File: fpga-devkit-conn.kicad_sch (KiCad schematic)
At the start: 12 parts, among them J13 PinHeader_2x10_P1.27mm_SMD_Sh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, J14 PinHeader_2x10_P1.27mm_SMD_Sh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

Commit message: [#83609] Reannotate board
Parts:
- renumbered J13 to J12, J14 to J13, R232 to R317, R233 to R318, R234 to R319, R235 to R320, R236 to R321, R237 to R322, R238 to R323, R239 to R324, R276 to R325, R277 to R326
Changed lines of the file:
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@@
 		(dnp no)
 		(fields_autoplaced yes)
-		(property "Reference" "J13"
+		(property "Reference" "J12"
 			(at 240.9825 173.99 0)
 			(effects
@@
 			(project "bmc-reference-carrier-board"
 				(path "/5f636c45-3c15-4731-8931-4625e0dab7e4/3ed11a6c-c41e-4496-8ded-d9f7860b25fe"
-					(reference "J13")
+					(reference "J12")
 					(unit 1)
 				)
@@
 		(on_board yes)
 		(dnp yes)
-		(property "Reference" "R232"
+		(property "Reference" "R317"
 			(at 150.368 90.424 0)
 			(effects
@@
 			(project "bmc-reference-carrier-board"
 				(path "/5f636c45-3c15-4731-8931-4625e0dab7e4/3ed11a6c-c41e-4496-8ded-d9f7860b25fe"
-					(reference "R232")
+					(reference "R317")
 					(unit 1)
 				)
@@
 		(on_board yes)
 		(dnp yes)
-		(property "Reference" "R236"
+		(property "Reference" "R321"
 			(at 150.368 105.664 0)
 			(effects
@@
 			(project "bmc-reference-carrier-board"
 				(path "/5f636c45-3c15-4731-8931-4625e0dab7e4/3ed11a6c-c41e-4496-8ded-d9f7860b25fe"
-					(reference "R236")
+					(reference "R321")
 					(unit 1)
 				)
@@
 		(on_board yes)
 		(dnp yes)
-		(property "Reference" "R276"
+		(property "Reference" "R325"
 			(at 165.1 221.615 0)
 			(effects
@@
 			(project "bmc-reference-carrier-board"
 				(path "/5f636c45-3c15-4731-8931-4625e0dab7e4/3ed11a6c-c41e-4496-8ded-d9f7860b25fe"
-					(reference "R276")
+					(reference "R325")
 					(unit 1)
 				)
@@
 		(on_board yes)
 		(dnp no)
-		(property "Reference" "#PWR0301"
+		(property "Reference" "#PWR0373"
 			(at 256.54 207.01 0)
 			(effects
@@
 			(project "bmc-reference-carrier-board"
 				(path "/5f636c45-3c15-4731-8931-4625e0dab7e4/3ed11a6c-c41e-4496-8ded-d9f7860b25fe"
-					(reference "#PWR0301")
+					(reference "#PWR0373")
 					(unit 1)
 				)
@@
 		(on_board yes)
 		(dnp no)
-		(property "Reference" "#PWR0270"
+		(property "Reference" "#PWR0374"
 			(at 259.08 119.38 0)
 			(effects
@@
 			(project "bmc-reference-carrier-board"
 				(path "/5f636c45-3c15-4731-8931-4625e0dab7e4/3ed11a6c-c41e-4496-8ded-d9f7860b25fe"
-					(reference "#PWR0270")
+					(reference "#PWR0374")
 					(unit 1)
 				)
@@
 		(on_board yes)
 		(dnp no)
-		(property "Reference" "#PWR0267"
+		(property "Reference" "#PWR0371"
 			(at 243.84 119.38 0)
 			(effects
@@
 			(project "bmc-reference-carrier-board"
 				(path "/5f636c45-3c15-4731-8931-4625e0dab7e4/3ed11a6c-c41e-4496-8ded-d9f7860b25fe"
-					(reference "#PWR0267")
+					(reference "#PWR0371")
 					(unit 1)
 				)
@@
 		(on_board yes)
 		(dnp yes)
-		(property "Reference" "R239"
+		(property "Reference" "R324"
 			(at 150.368 115.824 0)
 			(effects
@@
 			(project "bmc-reference-carrier-board"
 				(path "/5f636c45-3c15-4731-8931-4625e0dab7e4/3ed11a6c-c41e-4496-8ded-d9f7860b25fe"
-					(reference "R239")
+					(reference "R324")
 					(unit 1)
 				)
@@
 		(on_board yes)
 		(dnp yes)
-		(property "Reference" "R237"
+		(property "Reference" "R322"
 			(at 150.368 108.204 0)
 			(effects
@@
 			(project "bmc-reference-carrier-board"
 				(path "/5f636c45-3c15-4731-8931-4625e0dab7e4/3ed11a6c-c41e-4496-8ded-d9f7860b25fe"
-					(reference "R237")
+					(reference "R322")
 					(unit 1)
 				)
@@
 		(on_board yes)
 		(dnp yes)
-		(property "Reference" "R238"
+		(property "Reference" "R323"
 			(at 150.368 113.284 0)
 			(effects
@@
 			(project "bmc-reference-carrier-board"
 				(path "/5f636c45-3c15-4731-8931-4625e0dab7e4/3ed11a6c-c41e-4496-8ded-d9f7860b25fe"
-					(reference "R238")
+					(reference "R323")
 					(unit 1)
 				)
@@
 		(on_board yes)
 		(dnp yes)
-		(property "Reference" "R235"
+		(property "Reference" "R320"
 			(at 150.368 100.584 0)
 			(effects
@@
 			(project "bmc-reference-carrier-board"
 				(path "/5f636c45-3c15-4731-8931-4625e0dab7e4/3ed11a6c-c41e-4496-8ded-d9f7860b25fe"
-					(reference "R235")
+					(reference "R320")
 					(unit 1)
 				)
@@
 		(on_board yes)
 		(dnp yes)
-		(property "Reference" "R277"
+		(property "Reference" "R326"
 			(at 165.1 224.155 0)
 			(effects
@@
 			(project "bmc-reference-carrier-board"
 				(path "/5f636c45-3c15-4731-8931-4625e0dab7e4/3ed11a6c-c41e-4496-8ded-d9f7860b25fe"
-					(reference "R277")
+					(reference "R326")
 					(unit 1)
 				)
@@
 		(on_board yes)
 		(dnp yes)
-		(property "Reference" "R233"
+		(property "Reference" "R318"
 			(at 150.368 92.964 0)
 			(effects
@@
 			(project "bmc-reference-carrier-board"
 				(path "/5f636c45-3c15-4731-8931-4625e0dab7e4/3ed11a6c-c41e-4496-8ded-d9f7860b25fe"
-					(reference "R233")
+					(reference "R318")
 					(unit 1)
 				)
@@
 		(on_board yes)
 		(dnp yes)
-		(property "Reference" "R234"
+		(property "Reference" "R319"
 			(at 150.368 98.044 0)
 			(effects
@@
 			(project "bmc-reference-carrier-board"
 				(path "/5f636c45-3c15-4731-8931-4625e0dab7e4/3ed11a6c-c41e-4496-8ded-d9f7860b25fe"
-					(reference "R234")
+					(reference "R319")
 					(unit 1)
 				)
@@
 		(dnp no)
 		(fields_autoplaced yes)
-		(property "Reference" "J14"
+		(property "Reference" "J13"
 			(at 242.2525 85.09 0)
 			(effects
@@
 			(project "bmc-reference-carrier-board"
 				(path "/5f636c45-3c15-4731-8931-4625e0dab7e4/3ed11a6c-c41e-4496-8ded-d9f7860b25fe"
-					(reference "J14")
+					(reference "J13")
 					(unit 1)
 				)
@@
 		(on_board yes)
 		(dnp no)
-		(property "Reference" "#PWR0271"
+		(property "Reference" "#PWR0372"
 			(at 243.84 207.01 0)
 			(effects
@@
 			(project "bmc-reference-carrier-board"
 				(path "/5f636c45-3c15-4731-8931-4625e0dab7e4/3ed11a6c-c41e-4496-8ded-d9f7860b25fe"
-					(reference "#PWR0271")
+					(reference "#PWR0372")
 					(unit 1)
 				)

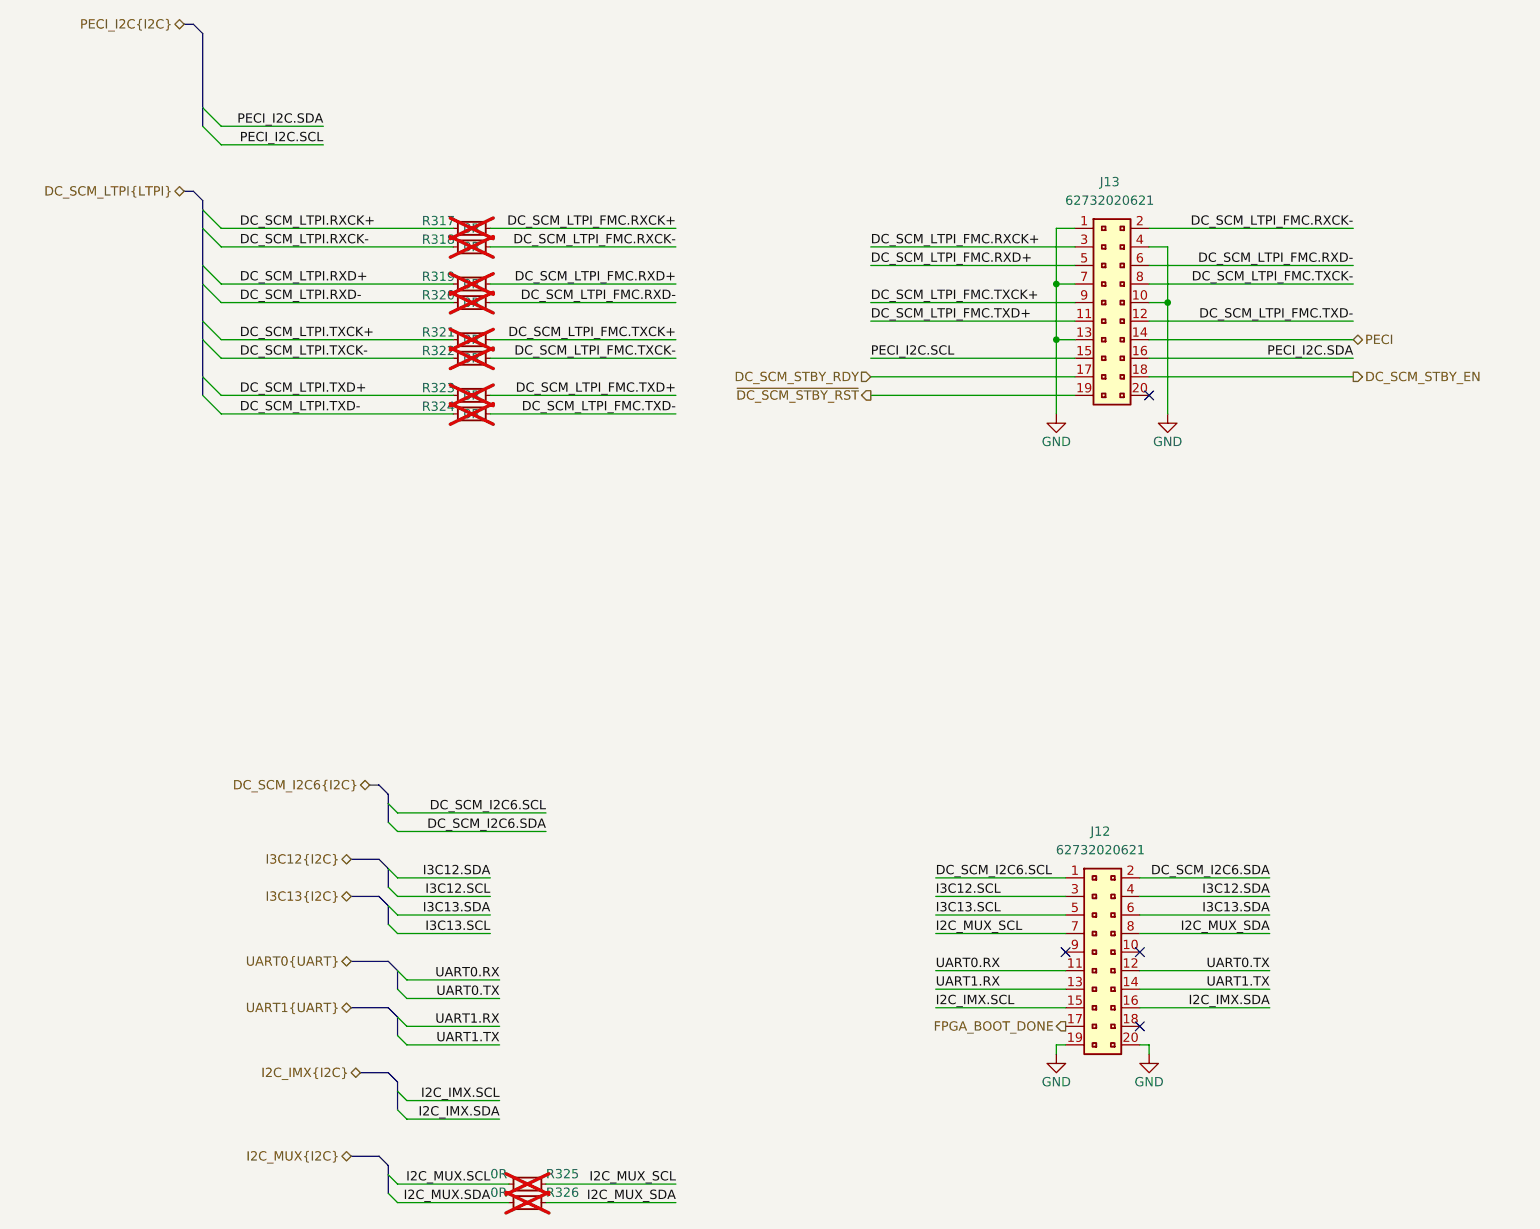
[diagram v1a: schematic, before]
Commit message: [#83736] Update devkit connectors pinout
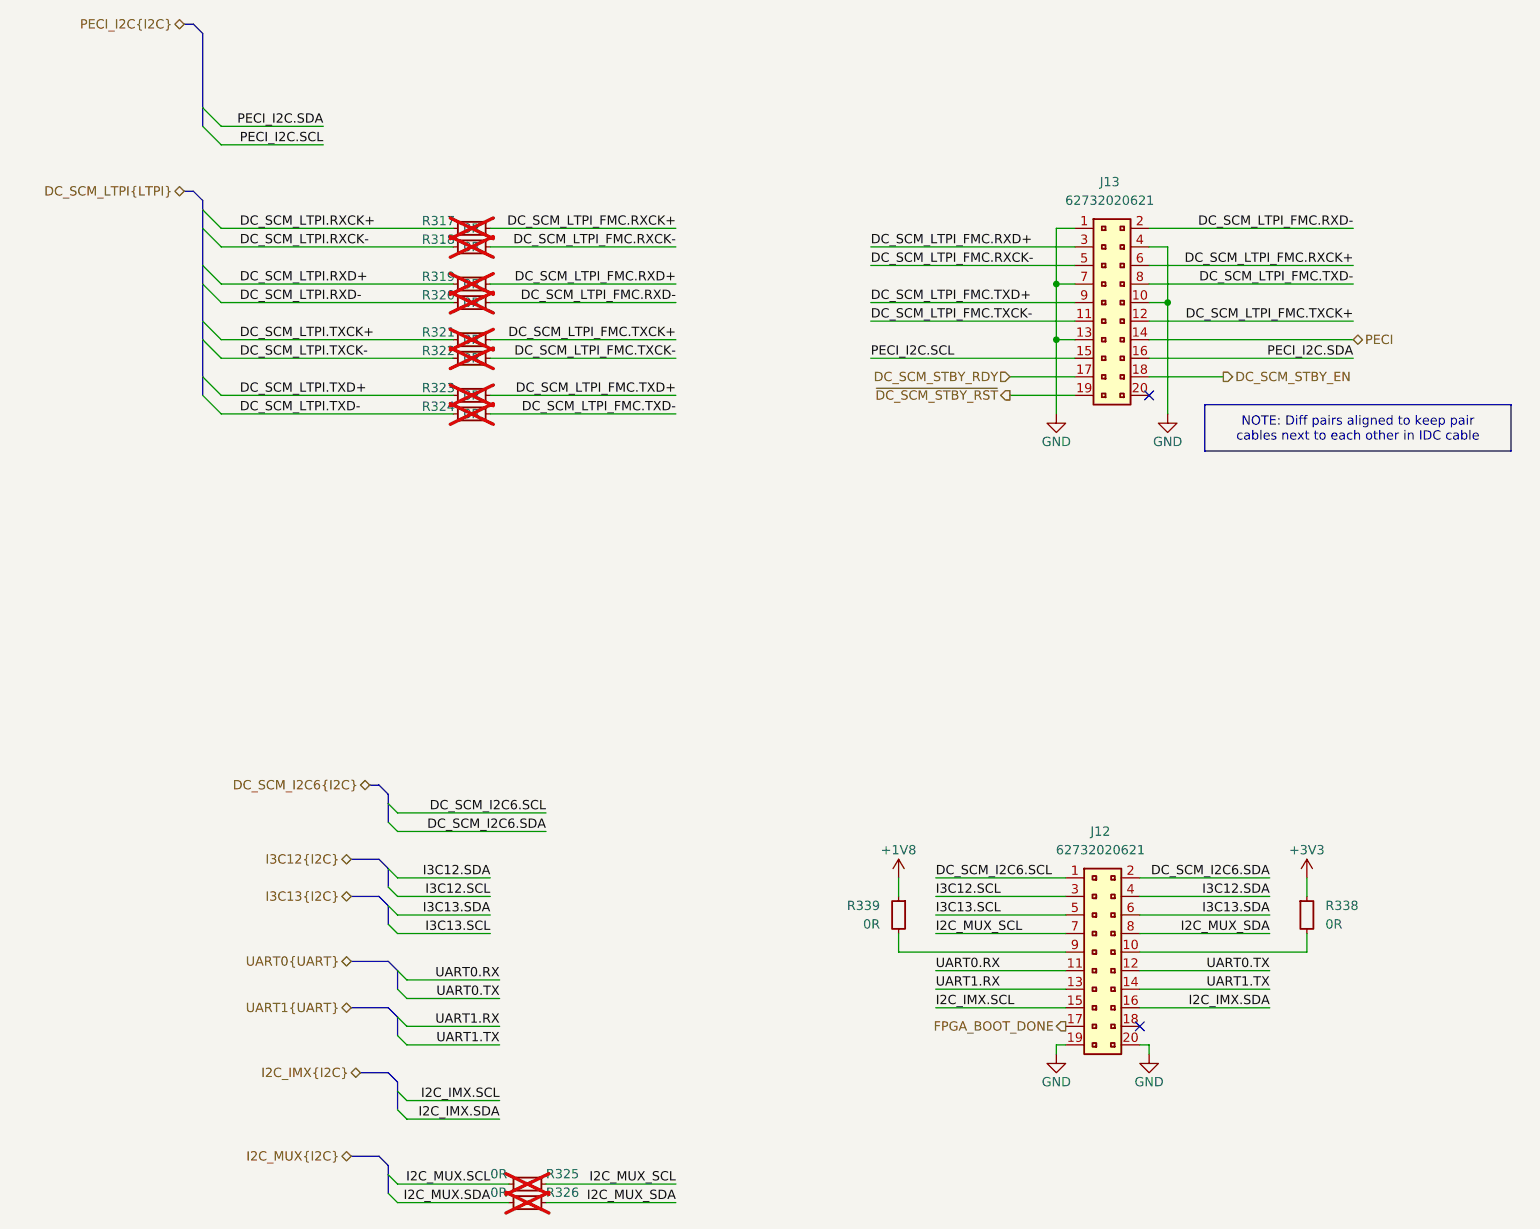
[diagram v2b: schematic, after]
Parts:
- added R338, R339: R_0R_0402, antmicro-footprints:R_0402_1005Metric, symbol antmicroResistors0402:R_0R_0402
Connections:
- net DC_SCM_LTPI_FMC.RXCK+: now also J13.6; no longer J13.3
- net DC_SCM_LTPI_FMC.RXCK-: now also J13.5; no longer J13.2
- net DC_SCM_LTPI_FMC.RXD+: now also J13.3; no longer J13.5
- net DC_SCM_LTPI_FMC.RXD-: now also J13.2; no longer J13.6
- net DC_SCM_LTPI_FMC.TXCK+: now also J13.12; no longer J13.9
- net DC_SCM_LTPI_FMC.TXCK-: now also J13.11; no longer J13.8
- net DC_SCM_LTPI_FMC.TXD+: now also J13.9; no longer J13.11
- net DC_SCM_LTPI_FMC.TXD-: now also J13.8; no longer J13.12
- net at J12.10: now also R338.2
- net at J12.9: now also R339.2
- new net +1V8: R339.1
- new net +3V3: R338.1
- no-connect marks 4 -> 2
